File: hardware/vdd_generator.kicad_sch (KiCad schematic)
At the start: 28 parts, among them Q1 BC547, Q2 BC327, Q3 BC327, Q4 BC327, U2 74LS06N

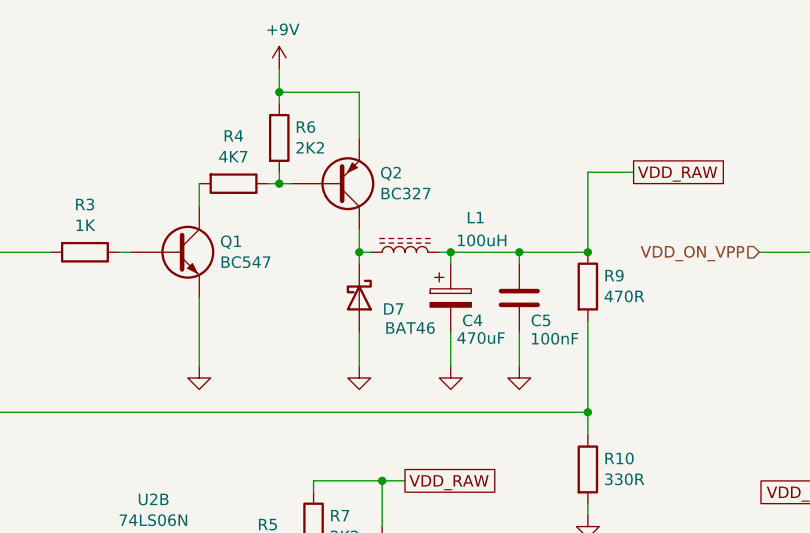
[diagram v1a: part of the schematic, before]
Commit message: Rev.G. Change external power supply to a MT3606 DC-DC Module
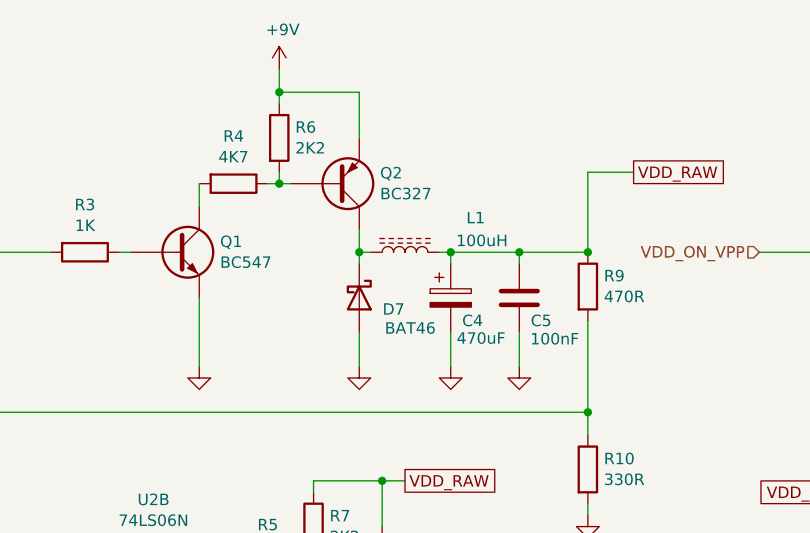
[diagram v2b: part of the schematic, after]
